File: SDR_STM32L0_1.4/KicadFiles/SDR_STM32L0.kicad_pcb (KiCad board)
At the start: 2 copper layers, 74 parts, among them J1 Conn_01x03, J2 USB_C_Receptacle_USB2.0_16P, J3 Conn_01x03, J4 Conn_01x03, J5 Conn_01x03, P1 3220-20-0200-00, SW1 SW_SPDT, SW2 RESET SWITCH, U1 MAX-8C-0-10, U2 Engine-Controller_SST25VF040B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, U3 STM32L083VBTx, U4 AMS1117-3.3, U5 CP2102N-Axx-xQFN28, U6 BMI323, U7 BMP390, Y1 32 MHz

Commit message: u
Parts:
- removed R20, R21: 33, Resistor_SMD:R_0612_1632Metric
- moved D2 79.8 mm to (99.0, 134.0)
- moved U5 77.5 mm to (104.5, 137.0)
- moved R2 76.8 mm to (103.0, 142.7), turned to 90 degrees
- moved C14 73.9 mm to (98.0, 138.6), turned to 90 degrees
- moved R4 73.7 mm to (105.0, 142.5), turned to 90 degrees
- moved H2 72.9 mm to (87.5, 150.0), turned to 90 degrees
- moved SW2 72.6 mm to (91.7, 126.5)
- moved JP1 72.1 mm to (96.5, 122.2), turned to 90 degrees
- moved J2 66.6 mm to (90.0, 139.0), turned to -90 degrees
- moved D3 65.6 mm to (96.5, 107.8), turned to 90 degrees
- moved R3 61.3 mm to (101.5, 142.5), turned to 90 degrees
- moved J3 61.2 mm to (85.7, 109.0), turned to 180 degrees
- moved C17 60.0 mm to (108.0, 111.0), turned to 180 degrees
- moved C16 59.8 mm to (108.5, 108.5), turned to 90 degrees
- moved J4 57.6 mm to (85.7, 113.5), turned to 180 degrees
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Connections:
- U3 pad 23: USART2_CTX -> USART2_CTS
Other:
- board outline added: 54 x 62 mm

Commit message: begin routing
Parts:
- SW2: footprint Button_Switch_THT:SW_DIP_SPSTx01_Slide_9.78x4.72mm_W7.62mm_P2.54mm -> Button_Switch_THT:SW_DIP_SPSTx01_Slide_6.7x4.1mm_W7.62mm_P2.54mm_LowProfile
- moved J4 41.8 mm to (122.4, 93.5), turned to -90 degrees
- moved C4 34.7 mm to (115.8, 131.8), turned to 180 degrees
- moved C5 29.6 mm to (104.8, 132.0), turned to 180 degrees
- moved C7 23.4 mm to (118.5, 114.0), turned to 180 degrees
- moved R4 16.6 mm to (93.5, 130.5), turned to 0 degrees
- moved R2 13.5 mm to (98.5, 130.0), turned to 180 degrees
- moved C11 10.0 mm to (87.0, 121.0)
- moved C8 9.80 mm to (102.5, 112.5)
- moved FB1 9.19 mm to (87.5, 125.5), turned to -90 degrees
- moved C3 8.96 mm to (100.5, 112.5)
- moved D2 7.70 mm to (106.5, 135.8), turned to 180 degrees
- moved C15 7.40 mm to (96.5, 144.0), turned to -90 degrees
- moved C2 7.09 mm to (96.6, 119.5), turned to -90 degrees
- moved R12 6.58 mm to (107.5, 111.0), turned to 0 degrees
- moved R3 5.83 mm to (96.5, 139.5)
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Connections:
- net SPI1_NSS renamed SPI1_NSS***********
- BT1 pad 2: Earth -> GND
- J1 pad 1: GPIO1_INPUT -> GPIO1_ADC
- J1 pad 3: GPIO1_ADC -> GPIO1_INPUT
- J3 pad 1: GPIO2_INPUT -> GPIO2_ADC
- J3 pad 3: GPIO2_ADC -> GPIO2_INPUT
- J4 pad 1: GPIO3_INPUT -> GPIO3_ADC
- J4 pad 3: GPIO3_ADC -> GPIO3_INPUT
- J5 pad 1: GPIO4_INPUT -> GPIO4_ADC
- J5 pad 3: GPIO4_ADC -> GPIO4_INPUT
- L1 pad 1: /Movement/GPS -> Net-(C20-Pad1)
- L1 pad 2: Net-(C20-Pad1) -> /Movement/GPS
- R17 pad 1: GPS_RST -> Net-(U1-~{RESET})
- R17 pad 2: Net-(U1-~{RESET}) -> GPS_RST
- R22 pad 2: USART2_TX -> USART1_TX
- R23 pad 2: USART2_RX -> USART1_RX
- U3 pad 70: USART1_CTS -> unconnected-(U3-PA11-Pad70)
- U6 pad 4: IMU_INPUT -> IMU_INPUT***
- U6 pad 9: IMU_OUTPUT -> IMU_OUTPUT***
- U7 pad 7: BP_INT -> BP_INT****
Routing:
- net +3.3V: track 0.00 -> 257.0 mm, vias 0 -> 6
- net GND: track 0.00 -> 73.9 mm, vias 0 -> 41
- net VBUS: track 0.00 -> 64.6 mm
- net NRST: track 0.00 -> 57.3 mm, vias 0 -> 4
- net USART2_TX: track 0.00 -> 32.9 mm, vias 0 -> 4
- net SYS_SWDIO: track 0.00 -> 32.5 mm, vias 0 -> 4
- net SPI1_SCK: track 0.00 -> 30.2 mm, vias 0 -> 2
- net SYS_SWCLK: track 0.00 -> 29.8 mm, vias 0 -> 2
- net Net-(U5-D-): track 0.00 -> 29.3 mm, vias 0 -> 2
- net LPTIM1_OUT: track 0.00 -> 26.5 mm, vias 0 -> 4
- net USART2_RX: track 0.00 -> 24.7 mm, vias 0 -> 2
- net I2C2_SCL: track 0.00 -> 24.5 mm, vias 0 -> 2
- net Net-(U1-~{SAFEBOOT}): track 0.00 -> 22.6 mm, vias 0 -> 2
- net USART2_CTS: track 0.00 -> 21.4 mm, vias 0 -> 4
- net Net-(U5-VBUS): track 0.00 -> 19.5 mm, vias 0 -> 2
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- added copper zone on B.Cu, net GND
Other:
- outline, holes or cut-outs redrawn

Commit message: Finished PCB Routing
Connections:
- R7 pad 2: SPI1_NSS*********** -> SPI1_NSS
- U2 pad 1: SPI1_NSS*********** -> SPI1_NSS
- U3 pad 11: unconnected-(U3-PH10-Pad11) -> GPIO4_INPUT
- U3 pad 16: LPTIM1_OUT -> LPUART1_TX
- U3 pad 17: unconnected-(U3-PC2-Pad17) -> GPIO4_ADC
- U3 pad 18: unconnected-(U3-PC3-Pad18) -> GPIO4_OUTPUT
- U3 pad 25: LPUART1_TX -> USART2_TX
- U3 pad 26: LPUART1_RX -> USART2_RX
- U3 pad 34: unconnected-(U3-PC5-Pad34) -> LPUART1_RX
- U3 pad 37: unconnected-(U3-PB2-Pad37) -> LPTIM1_OUT
- U3 pad 41: unconnected-(U3-PE10-Pad41) -> SPI1_NSS
- U3 pad 46: unconnected-(U3-PE15-Pad46) -> BP_INT
- U3 pad 52: unconnected-(U3-PB13-Pad52) -> GPIO1_INPUT
- U3 pad 53: unconnected-(U3-PB14-Pad53) -> GPIO1_OUTPUT
- U3 pad 54: unconnected-(U3-PB15-Pad54) -> GPIO1_ADC
- U3 pad 60: GPIO1_ADC -> unconnected-(U3-PD13-Pad60)
- U3 pad 61: GPIO1_OUTPUT -> unconnected-(U3-PD14-Pad61)
- U3 pad 62: GPIO1_INPUT -> unconnected-(U3-PD15-Pad62)
- U3 pad 64: GPIO4_INPUT -> unconnected-(U3-PC7-Pad64)
- U3 pad 65: GPIO4_OUTPUT -> unconnected-(U3-PC8-Pad65)
- U3 pad 66: GPIO4_ADC -> unconnected-(U3-PC9-Pad66)
- U3 pad 71: unconnected-(U3-PA12-Pad71) -> GPS_TIM
- U3 pad 77: USART2_RX -> unconnected-(U3-PA15-Pad77)
- U3 pad 78: GPIO3_INPUT -> unconnected-(U3-PC10-Pad78)
- U3 pad 79: GPIO3_OUTPUT -> unconnected-(U3-PC11-Pad79)
- U3 pad 80: GPIO3_ADC -> unconnected-(U3-PC12-Pad80)
- U3 pad 81: unconnected-(U3-PD0-Pad81) -> GPIO3_INPUT
- U3 pad 82: unconnected-(U3-PD1-Pad82) -> GPIO3_OUTPUT
- U3 pad 83: unconnected-(U3-PD2-Pad83) -> GPIO3_ADC
- U3 pad 86: USART2_TX -> unconnected-(U3-PD5-Pad86)
- U3 pad 87: GPS_TIM -> unconnected-(U3-PD6-Pad87)
- U3 pad 88: BP_INT -> unconnected-(U3-PD7-Pad88)
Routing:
- net GPIO4_OUTPUT: track 0.00 -> 38.2 mm, vias 0 -> 4
- net GPIO4_ADC: track 0.00 -> 37.9 mm, vias 0 -> 2
- net GPIO2_ADC: track 0.00 -> 37.6 mm, vias 0 -> 4
- net GPIO2_OUTPUT: track 0.00 -> 32.6 mm, vias 0 -> 2
- net GPIO1_OUTPUT: track 0.00 -> 30.6 mm, vias 0 -> 2
- net GPIO3_ADC: track 0.00 -> 29.1 mm, vias 0 -> 2
- net GPIO4_INPUT: track 0.00 -> 27.9 mm, vias 0 -> 2
- net +3.3V: track 257.0 -> 284.1 mm, vias 6 -> 8
- net GPIO3_OUTPUT: track 0.00 -> 25.2 mm, vias 0 -> 4
- net GPIO3_INPUT: track 0.00 -> 24.7 mm, vias 0 -> 4
- net GPIO1_INPUT: track 0.00 -> 22.8 mm, vias 0 -> 2
- net GND: track 73.9 -> 96.3 mm, vias 41 -> 43
- net GPIO2_INPUT: track 0.00 -> 22.1 mm, vias 0 -> 2
- net GPIO1_ADC: track 0.00 -> 18.4 mm, vias 0 -> 2
- net USART2_TX: track 32.9 -> 49.3 mm, vias 4 -> 2
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
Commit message: 1.5
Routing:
- net +3.3V: track 284.1 -> 295.2 mm, vias 8 -> 10
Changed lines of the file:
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@@
 		(layer "Edge.Cuts")
 	)
+	(dimension
+		(type aligned)
+		(layer "B.Cu")
+		(pts
+			(xy 84.5 91) (xy 84.5 153)
+		)
+		(height 1.749999)
+		(gr_text "2.4409 in"
+			(at 80.950001 122 90)
+			(layer "B.Cu")
+			(effects
+				(font
+					(size 1.5 1.5)
+					(thickness 0.3)
+				)
+			)
+		)
+		(format
+			(prefix "")
+			(suffix "")
+			(units 3)
+			(units_format 1)
+			(precision 4)
+		)
+		(style
+			(thickness 0.2)
+			(arrow_length 1.27)
+			(text_position_mode 0)
+			(extension_height 0.58642)
+			(extension_offset 0.5) keep_text_aligned)
+	)
+	(dimension
+		(type aligned)
+		(layer "B.Cu")
+		(pts
+			(xy 84.5 91) (xy 138.5 91)
+		)
+		(height -1.5)
+		(gr_text "2.1260 in"
+			(at 111.5 87.7 0)
+			(layer "B.Cu")
+			(effects
+				(font
+					(size 1.5 1.5)
+					(thickness 0.3)
+				)
+			)
+		)
+		(format
+			(prefix "")
+			(suffix "")
+			(units 3)
+			(units_format 1)
+			(precision 4)
+		)
+		(style
+			(thickness 0.2)
+			(arrow_length 1.27)
+			(text_position_mode 0)
+			(extension_height 0.58642)
+			(extension_offset 0.5) keep_text_aligned)
+	)
 	(segment
 		(start 106 110.98)
@@
 	)
 	(segment
+		(start 98.5 104)
+		(end 92 104)
+		(width 0.5)
+		(layer "F.Cu")
+		(net 6)
+	)
+	(segment
 		(start 107 104)
 		(end 103.5 104)
@@
 	)
 	(segment
-		(start 103.5 104)
-		(end 92 104)
-		(width 0.5)
-		(layer "F.Cu")
-		(net 6)
-	)
-	(segment
 		(start 98 142.5)
 		(end 98 143.5)
@@
 	)
 	(segment
+		(start 98.5 104)
+		(end 98.5 103.25)
+		(width 0.5)
+		(layer "F.Cu")
+		(net 6)
+	)
+	(segment
 		(start 99 137.2)
 		(end 99 135.5)
@@
 	)
 	(segment
+		(start 100.43295 99.56705)
+		(end 103.07 99.56705)
+		(width 0.5)
+		(layer "F.Cu")
+		(net 6)
+	)
+	(segment
 		(start 95 141)
 		(end 96.5 141)
@@
 	)
 	(segment
+		(start 100.43295 99.56705)
+		(end 101.70295 98.29705)
+		(width 0.5)
+		(layer "F.Cu")
+		(net 6)
+	)
+	(segment
 		(start 124 143.075)
 		(end 122.5 141.575)
@@
 	)
 	(segment
+		(start 103.5 104)
+		(end 98.5 104)
+		(width 0.5)
+		(layer "F.Cu")
+		(net 6)
+	)
+	(segment
 		(start 99.5 137.2)
 		(end 99.5 136.5)
@@
 	)
 	(segment
+		(start 101.70295 98.29705)
+		(end 103.07 98.29705)
+		(width 0.5)
+		(layer "F.Cu")
+		(net 6)
+	)
+	(segment
 		(start 110.500001 110.6626)
 		(end 110.4356 110.727001)
@@
 	)
 	(segment
+		(start 98.5 101.5)
+		(end 100.43295 99.56705)
+		(width 0.5)
+		(layer "F.Cu")
+		(net 6)
+	)
+	(segment
 		(start 114 104)
 		(end 107.5 104)
@@
 	)
 	(via
+		(at 98.5 103.25)
+		(size 0.6)
+		(drill 0.3)
+		(layers "F.Cu" "B.Cu")
+		(net 6)
+	)
+	(via
 		(at 130.5 117.5)
 		(size 0.7)
@@
 	)
 	(via
+		(at 98.5 101.5)
+		(size 0.6)
+		(drill 0.3)
+		(layers "F.Cu" "B.Cu")
+		(net 6)
+	)
+	(via
 		(at 110.15 136)
 		(size 0.6)
@@
 	)
 	(segment
+		(start 98.5 103.25)
+		(end 98.5 101.5)
+		(width 0.5)
+		(layer "B.Cu")
+		(net 6)
+	)
+	(segment
 		(start 110.5 138.5)
 		(end 110.5 136.5)
@@
 	)
 	(segment
+		(start 91 104.151472)
+		(end 91 119)
+		(width 0.3)
+		(layer "F.Cu")
+		(net 8)
+	)
+	(segment
+		(start 96.75 103)
+		(end 92.151472 103)
+		(width 0.3)
+		(layer "F.Cu")
+		(net 8)
+	)
+	(segment
 		(start 97.9775 121.9775)
 		(end 97.9775 121.5)
@@
 	)
 	(segment
-		(start 92.151472 103)
-		(end 91 104.151472)
-		(width 0.3)
-		(layer "F.Cu")
-		(net 8)
-	)
-	(segment
 		(start 98.53 122.53)
 		(end 97.62 123.44)
@@
 	)
 	(segment
-		(start 91 119)
-		(end 91.5 119)
+		(start 92.151472 103)
+		(end 91 104.151472)
 		(width 0.3)
 		(layer "F.Cu")
@@
 	)
 	(segment
-		(start 91 104.151472)
-		(end 91 119)
+		(start 98.5 122.5)
+		(end 98.53 122.53)
 		(width 0.3)
 		(layer "F.Cu")
@@
 	)
 	(segment
-		(start 102 102.470366)
-		(end 102 103)
+		(start 103.470366 101)
+		(end 102.220366 102.25)
 		(width 0.3)
 		(layer "F.Cu")
@@
 	)
 	(segment
-		(start 98.5 122.5)
-		(end 98.53 122.53)
+		(start 97.62 123.44)
+		(end 97.62 125)
 		(width 0.3)
 		(layer "F.Cu")
@@
 	)
 	(segment
-		(start 97.62 123.44)
-		(end 97.62 125)
+		(start 102.220366 102.25)
+		(end 97.5 102.25)
 		(width 0.3)
 		(layer "F.Cu")
@@
 	)
 	(segment
-		(start 103.470366 101)
-		(end 102 102.470366)
+		(start 97.5 102.25)
+		(end 96.75 103)
 		(width 0.3)
 		(layer "F.Cu")
@@
 	)
 	(segment
-		(start 102 103)
-		(end 92.151472 103)
+		(start 105 101)
+		(end 103.470366 101)
 		(width 0.3)
 		(layer "F.Cu")
@@
 	)
 	(segment
-		(start 105 101)
-		(end 103.470366 101)
+		(start 91 119)
+		(end 91.5 119)
 		(width 0.3)
 		(layer "F.Cu")
@@
 	)
 	(segment
-		(start 113.332705 134.35)
-		(end 113.822113 134.839408)
+		(start 111.9 139.1)
+		(end 108.190381 139.1)
 		(width 0.2)
 		(layer "B.Cu")
@@
 	)
 	(segment
-		(start 106.85 139.65)
+		(start 107.430761 139.65)
 		(end 105.15 139.65)
 		(width 0.2)
@@
 	)
 	(segment
-		(start 107.4 139.1)
-		(end 106.85 139.65)
+		(start 113.332705 134.35)
+		(end 113.822113 134.839408)
+		(width 0.2)
+		(layer "B.Cu")
+		(net 73)
+	)
+	(segment
+		(start 105.15 139.65)
+		(end 105 139.5)
 		(width 0.2)
 		(layer "B.Cu")
@@
 	)
 	(segment
-		(start 110.5 134.35)
-		(end 113.332705 134.35)
+		(start 107.730761 139.35)
+		(end 107.430761 139.65)
 		(width 0.2)
 		(layer "B.Cu")
@@
 	)
 	(segment
-		(start 108.22 132.172607)
-		(end 110.397393 134.35)
+		(start 107.940381 139.35)
+		(end 107.730761 139.35)
 		(width 0.2)
 		(layer "B.Cu")
@@
 	)
 	(segment
-		(start 105.15 139.65)
-		(end 105 139.5)
+		(start 110.5 134.35)
+		(end 113.332705 134.35)
 		(width 0.2)
 		(layer "B.Cu")
@@
 	)
 	(segment
-		(start 111.9 139.1)
-		(end 107.4 139.1)
+		(start 108.22 132.172607)
+		(end 110.397393 134.35)
+		(width 0.2)
+		(layer "B.Cu")
+		(net 73)
+	)
+	(segment
+		(start 108.190381 139.1)
+		(end 107.940381 139.35)
 		(width 0.2)
 		(layer "B.Cu")

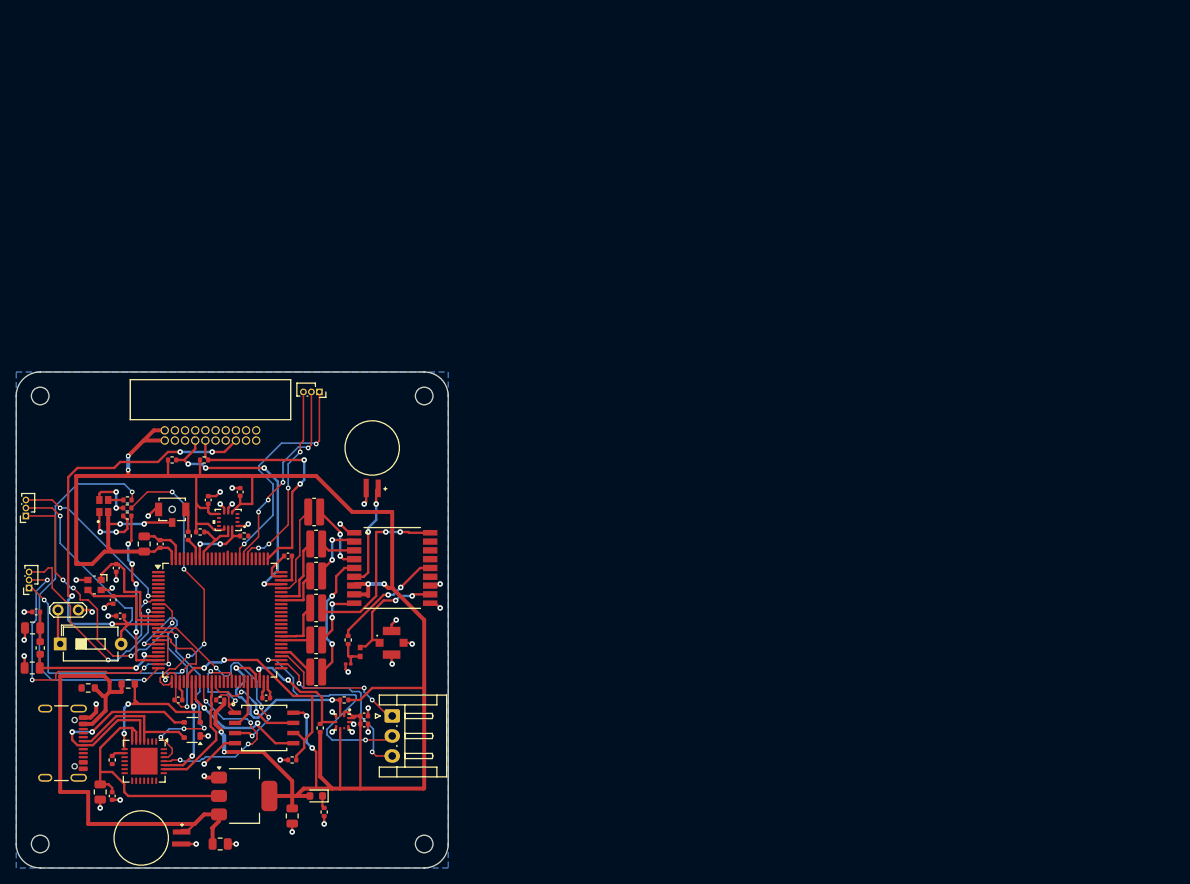
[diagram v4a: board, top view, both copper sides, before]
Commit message: Upgrade
Changed a few peripherals (less ports, +/- on ports, switched jumpers, switched pinouts), and made new shematic
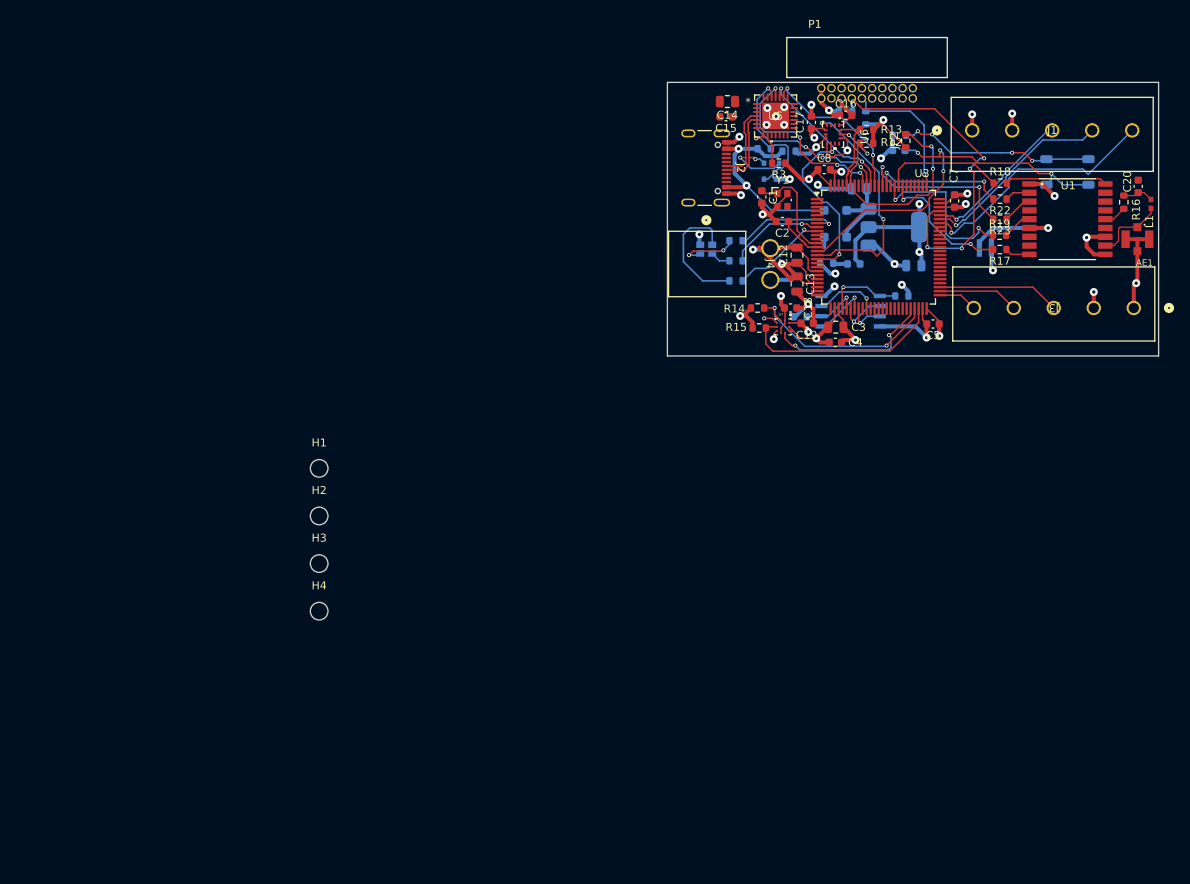
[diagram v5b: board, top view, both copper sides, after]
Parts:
- removed 10k1: R, Resistor_SMD:R_0402_1005Metric
- removed BT2: 5V Battery, FlightComputer:MS621FE-FL11E
- removed C11: 10n, Capacitor_SMD:C_0402_1005Metric
- removed FB1: 120R, Inductor_SMD:L_0603_1608Metric
- removed J5: Conn_01x03, Connector_PinSocket_1.00mm:PinSocket_1x03_P1.00mm_Vertical
- removed R24: 33, Resistor_SMD:R_0612_1632Metric
- removed SW1: SW_SPDT, Button_Switch_SMD:SW_SPST_B3U-1100P-B
- added D4: 5V, Diode_SMD:D_SOD-123F, B.Cu at (186.9, 70.8)
- added D5: 5V, Diode_SMD:D_SOD-123F, B.Cu at (186.9, 74.2)
- added JP2: Open Jumper, Resistor_SMD:R_0603_1608Metric, F.Cu at (195.7, 62.1)
- AE1: footprint FlightComputer:73412-0110 -> FCMac:73412-0110
- BT1: footprint FlightComputer:MS621FE-FL11E -> FCMac:MS621FE-FL11E; moved to B.Cu
- C1, C2: value 70pF -> 25pF; footprint Capacitor_SMD:C_0402_1005Metric -> Capacitor_SMD:C_0603_1608Metric
- C10, D1, D2, R2, R4, U4: moved to B.Cu
- C13: value 1u -> 0.1u
- C15, C16, C17, C18, C19, C4, C5, C7, C8: footprint Capacitor_SMD:C_0402_1005Metric -> Capacitor_SMD:C_0603_1608Metric
- C20: footprint Capacitor_SMD:C_0201_0603Metric -> Capacitor_SMD:C_0603_1608Metric
- C6: value 22u -> 10u; moved to B.Cu
- C9: footprint Capacitor_SMD:C_0402_1005Metric -> Capacitor_SMD:C_0603_1608Metric; moved to B.Cu
- D3: footprint FlightComputer:CLMVC-FKA-CL1D1L71BB7C3C3 -> FCMac:CLMVC-FKA-CL1D1L71BB7C3C3; moved to B.Cu
- J1: value Conn_01x03 -> Conn_01x05_Pin; footprint Connector_JST:JST_EH_S3B-EH_1x03_P2.50mm_Horizontal -> 19351990:CONN_1935190_PXC
- J3: value Conn_01x03 -> Conn_01x05_Pin; footprint Connector_PinSocket_1.00mm:PinSocket_1x03_P1.00mm_Vertical -> 19351990:CONN_1935190_PXC
- J4: value Conn_01x03 -> Conn_01x02_Pin; footprint Connector_PinSocket_1.00mm:PinSocket_1x03_P1.00mm_Vertical -> 647676_2:CONN2_647676-2_TEC
- JP1: footprint TestPoint:TestPoint_2Pads_Pitch2.54mm_Drill0.8mm -> Resistor_SMD:R_0603_1608Metric; moved to B.Cu
- L1: footprint FlightComputer:L-07C27NJV6T -> FCMac:L-07C27NJV6T
- P1: footprint FlightComputer:3220-20-0200-00 -> FCMac:3220-20-0200-00
- R1, R10, R11, R5, R6, R7, R8, R9: footprint Resistor_SMD:R_0402_1005Metric -> Resistor_SMD:R_0603_1608Metric; moved to B.Cu
- R12, R13, R14, R15, R16, R3: footprint Resistor_SMD:R_0402_1005Metric -> Resistor_SMD:R_0603_1608Metric
- R17, R18, R19, R22, R23: footprint Resistor_SMD:R_0612_1632Metric -> Resistor_SMD:R_0603_1608Metric
- SW2: footprint Button_Switch_THT:SW_DIP_SPSTx01_Slide_6.7x4.1mm_W7.62mm_P2.54mm_LowProfile -> Button_Switch_SMD:SW_SPST_PTS647_Sx38; moved to B.Cu
- U1: footprint FlightComputer:MAX-8C-0 -> FCMac:MAX-8C-0
- U2: footprint FlightComputer:SST25VF040B-50-4I-S2AE-T -> FCMac:SST25VF040B-50-4I-S2AE-T; moved to B.Cu
- U5: footprint Package_DFN_QFN:QFN-28-1EP_5x5mm_P0.5mm_EP3.35x3.35mm -> CP2102N:QFN28_5X5_SIL
- U6: footprint FlightComputer:BMI323 -> FCMac:BMI323
- U7: footprint FlightComputer:BMP390 -> FCMac:BMP390
- Y1: value 32 MHz -> 25 MHz
- moved J3 140.9 mm to (224.2, 83.0)
- moved SW2 139.0 mm to (215.9, 66.0), turned to 180 degrees
- moved JP1 118.6 mm to (194.9, 61.4), turned to 0 degrees
- moved C14 116.6 mm to (173.4, 57.2), turned to 180 degrees
- moved C20 115.4 mm to (224.8, 67.8), turned to 90 degrees
- moved C15 114.4 mm to (173.2, 59.1), turned to 180 degrees
- moved C6 114.4 mm to (189.9, 68.1), turned to 180 degrees
- moved L1 113.6 mm to (226.3, 70.0), turned to -90 degrees
- moved C9 113.4 mm to (194.8, 63.3)
- moved U5 112.8 mm to (179.4, 59.0), turned to 0 degrees
- moved R3 111.8 mm to (179.8, 64.9), turned to 180 degrees
- moved R16 111.3 mm to (222.9, 69.8), turned to -90 degrees
- moved R4 110.3 mm to (181.1, 63.4), turned to 180 degrees
- moved U4 107.9 mm to (194.2, 72.9)
- moved J2 107.9 mm to (169.6, 65.5)
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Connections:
- C12 pad 1: Net-(C11-Pad1) -> +3.3V
- C13 pad 1: +3.3VA -> +3.3V
- C6 pad 1: VBUS -> Net-(D4-K)
- J1 pad 1: GPIO1_ADC -> GND
- J1 pad 2: GPIO1_OUTPUT -> +3.3V
- J1 pad 3: GPIO1_INPUT -> GPIO4_INPUT
- J3 pad 1: GPIO2_ADC -> GND
- J3 pad 2: GPIO2_OUTPUT -> +3.3V
- J3 pad 3: GPIO2_INPUT -> GPIO3_INPUT
- J4 pad 1: GPIO3_ADC -> GND
- J4 pad 2: GPIO3_OUTPUT -> Net-(D5-A)
- R10 pad 2: USART2_RX -> GOUTPUT
- R11 pad 2: USART2_TX -> BOUTPUT
- R17 pad 2: GPS_RST -> GPIO_GPSRST
- R18 pad 1: GPS_SBOOT -> GPIO_GPSSB
- R19 pad 1: GPS_INT -> EXTI_13
- R22 pad 2: USART1_TX -> USART2_TX
- R23 pad 2: USART1_RX -> USART2_RX
- R9 pad 2: USART2_CTS -> ROUTPUT
- U2 pad 3: LPTIM1_IN -> GPIO_OUTFL
- U2 pad 7: LPTIM1_OUT -> TIM3_CH3
- U3 pad 1: unconnected-(U3-PE2-Pad1) -> GPIO1_INPUT
- U3 pad 11: GPIO4_INPUT -> unconnected-(U3-PH10-Pad11)
- U3 pad 15: LPTIM1_IN -> EXTI_10
- U3 pad 16: LPUART1_TX -> EXTI_11
- U3 pad 17: GPIO4_ADC -> unconnected-(U3-PC2-Pad17)
- U3 pad 18: GPIO4_OUTPUT -> unconnected-(U3-PC3-Pad18)
- U3 pad 2: unconnected-(U3-PE3-Pad2) -> GPIO1_OUTPUT
- U3 pad 22: +3.3VA -> +3.3V
- U3 pad 23: USART2_CTS -> GPIO2_INPUT
- U3 pad 24: unconnected-(U3-PA1-Pad24) -> GPIO2_OUTPUT
- U3 pad 25: USART2_TX -> GPIO2_ADC
- U3 pad 26: USART2_RX -> unconnected-(U3-PA3-Pad26)
- U3 pad 29: unconnected-(U3-PA4-Pad29) -> SPI1_NSS
- U3 pad 3: unconnected-(U3-PE4-Pad3) -> GPIO1_ADC
- U3 pad 31: LPUART1_CTS -> SPI1_MISO
- U3 pad 33: unconnected-(U3-PC4-Pad33) -> GPIO_OUTFL
- U3 pad 34: LPUART1_RX -> unconnected-(U3-PC5-Pad34)
- U3 pad 35: unconnected-(U3-PB0-Pad35) -> TIM3_CH3
- U3 pad 36: LPUART1_RTS -> unconnected-(U3-PB1-Pad36)
- U3 pad 37: LPTIM1_OUT -> unconnected-(U3-PB2-Pad37)
- U3 pad 41: SPI1_NSS -> unconnected-(U3-PE10-Pad41)
- U3 pad 45: SPI1_MISO -> unconnected-(U3-PE14-Pad45)
- U3 pad 46: BP_INT -> EXTI_15
- U3 pad 51: unconnected-(U3-PB12-Pad51) -> GPIO3_ADC
- U3 pad 52: GPIO1_INPUT -> GPIO3_OUTPUT
- U3 pad 53: GPIO1_OUTPUT -> GPIO3_INPUT
- U3 pad 54: GPIO1_ADC -> unconnected-(U3-PB15-Pad54)
- U3 pad 55: GPS_INT -> unconnected-(U3-PD8-Pad55)
- U3 pad 56: IMU_INPUT -> unconnected-(U3-PD9-Pad56)
- U3 pad 57: IMU_OUTPUT -> unconnected-(U3-PD10-Pad57)
- U3 pad 58: GPS_RST -> unconnected-(U3-PD11-Pad58)
- U3 pad 59: GPS_SBOOT -> unconnected-(U3-PD12-Pad59)
- U3 pad 68: USART1_TX -> unconnected-(U3-PA9-Pad68)
- U3 pad 69: USART1_RX -> GPIO4_ADC
- U3 pad 7: GPIO2_INPUT -> ROUTPUT
- U3 pad 70: unconnected-(U3-PA11-Pad70) -> GPIO4_OUTPUT
- U3 pad 71: GPS_TIM -> GPIO4_INPUT
- U3 pad 8: GPIO2_OUTPUT -> GOUTPUT
- U3 pad 81: GPIO3_INPUT -> unconnected-(U3-PD0-Pad81)
- U3 pad 82: GPIO3_OUTPUT -> GPIO_GPSRST
- U3 pad 83: GPIO3_ADC -> GPIO_GPSSB
- U3 pad 84: unconnected-(U3-PD3-Pad84) -> EXTI_13
- U3 pad 85: unconnected-(U3-PD4-Pad85) -> EXTI_14
- U3 pad 86: unconnected-(U3-PD5-Pad86) -> USART2_TX
- U3 pad 87: unconnected-(U3-PD6-Pad87) -> USART2_RX
- U3 pad 89: unconnected-(U3-PB3-Pad89) -> USART1_RTS
- U3 pad 9: GPIO2_ADC -> BOUTPUT
- U3 pad 90: unconnected-(U3-PB4-Pad90) -> USART1_CTS
- U3 pad 91: unconnected-(U3-PB5-Pad91) -> USART1_TX
- U3 pad 92: I2C1_SCL -> USART1_RX
- U3 pad 93: I2C1_SDA -> unconnected-(U3-PB7-Pad93)
- U3 pad 95: unconnected-(U3-PB8-Pad95) -> I2C1_SCL
- U3 pad 96: unconnected-(U3-PB9-Pad96) -> I2C1_SDA
- U4 pad 3: VBUS -> Net-(D4-K)
- U5 pad 23: LPUART1_RTS -> USART1_RTS
- U5 pad 24: LPUART1_CTS -> USART1_CTS
- U5 pad 25: LPUART1_RX -> USART1_RX
- U5 pad 26: LPUART1_TX -> USART1_TX
- U6 pad 4: IMU_INPUT*** -> EXTI_10
- U6 pad 9: IMU_OUTPUT*** -> EXTI_11
- U7 pad 7: BP_INT**** -> EXTI_15
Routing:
- net +3.3V: track 295.2 -> 103.1 mm, vias 10 -> 19
- net VBUS: track 64.6 -> 26.7 mm, vias 0 -> 2
- net GPIO2_ADC: track 37.6 -> 0.00 mm, vias 4 -> 0
- net GPIO2_OUTPUT: track 32.6 -> 0.00 mm, vias 2 -> 0
- net USART2_TX: track 49.3 -> 16.9 mm
- net GPIO1_OUTPUT: track 30.6 -> 0.00 mm, vias 2 -> 0
- net EXTI_10: track 0.00 -> 29.6 mm, vias 0 -> 2
- net GND: track 96.3 -> 125.5 mm, vias 43 -> 28
- net LPTIM1_IN: track 28.1 -> 0.00 mm, vias 4 -> 0
- net LPUART1_TX: track 25.5 -> 0.00 mm, vias 4 -> 0
- net LPUART1_RX: track 24.6 -> 0.00 mm, vias 4 -> 0
- net GPIO3_ADC: track 29.1 -> 4.88 mm, vias 2 -> 0
- net GPIO1_INPUT: track 22.8 -> 0.00 mm, vias 2 -> 0
- net SPI1_SCK: track 29.6 -> 7.34 mm, vias 2 -> 1
- net GPIO2_INPUT: track 22.1 -> 0.00 mm, vias 2 -> 0
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- added copper zone on In2.Cu, net +3.3V
- added copper zone on In1.Cu, net GND
- removed copper zone on B.Cu, net GND
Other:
- board size 54 x 62 mm -> 61.4 x 34.2 mm
- copper layers 2 -> 4
- board text added: "ACD Out In + -"
